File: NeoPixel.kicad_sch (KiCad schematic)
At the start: 2 parts

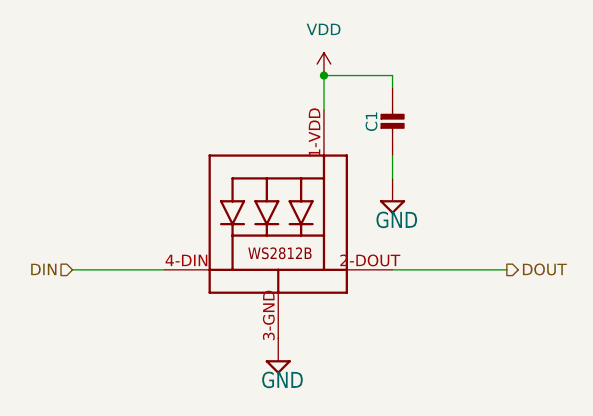
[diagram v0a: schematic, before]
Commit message: Libraries corrected, references updated
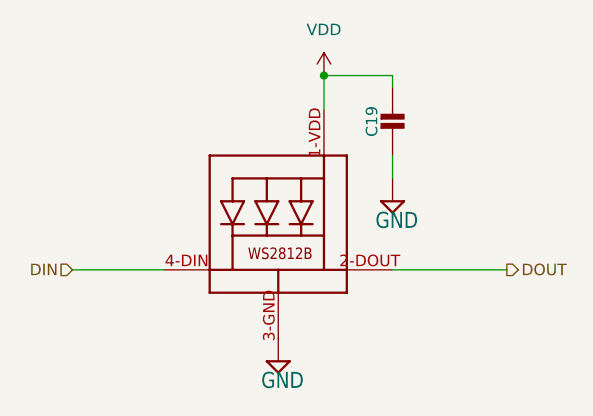
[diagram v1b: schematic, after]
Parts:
- renumbered C1 to C19, LED1 to LED19
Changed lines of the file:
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@@
 		(on_board yes)
 		(dnp no)
-		(property "Reference" "#SUPPLY031"
+		(property "Reference" "#SUPPLY038"
 			(at 151.13 95.25 0)
 			(effects
@@
 		(on_board yes)
 		(dnp no)
-		(property "Reference" "LED1"
+		(property "Reference" "LED19"
 			(at 138.43 100.33 0)
 			(effects
@@
 		(on_board yes)
 		(dnp no)
-		(property "Reference" "#SUPPLY015"
+		(property "Reference" "#SUPPLY037"
 			(at 138.43 113.03 0)
 			(effects
@@
 		(on_board yes)
 		(dnp no)
-		(property "Reference" "C1"
+		(property "Reference" "C19"
 			(at 148.84 86.38 90)
 			(effects
@@
 		(dnp no)
 		(fields_autoplaced yes)
-		(property "Reference" "#PWR04"
+		(property "Reference" "#PWR020"
 			(at 143.51 85.09 0)
 			(effects
@@
 					(unit 1)
 				)
+				(path "/e63d8811-5bec-4b10-b8d5-5521494324c3/128f7785-7fd0-431a-8484-daa6f8c7bf32"
+					(reference "#PWR?")
+					(unit 1)
+				)
